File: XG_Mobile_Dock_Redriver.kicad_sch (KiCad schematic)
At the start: 158 parts, among them J1 5-1775443-8, J13 39301240, J14 I2C1, J2 20455-040E-76, J3 20455-040E-76, J6 455860005, J7 10147430-113T0LF, SW1 SW_Push, U1 DS320PR810NJXR, U2 DS320PR810NJXR

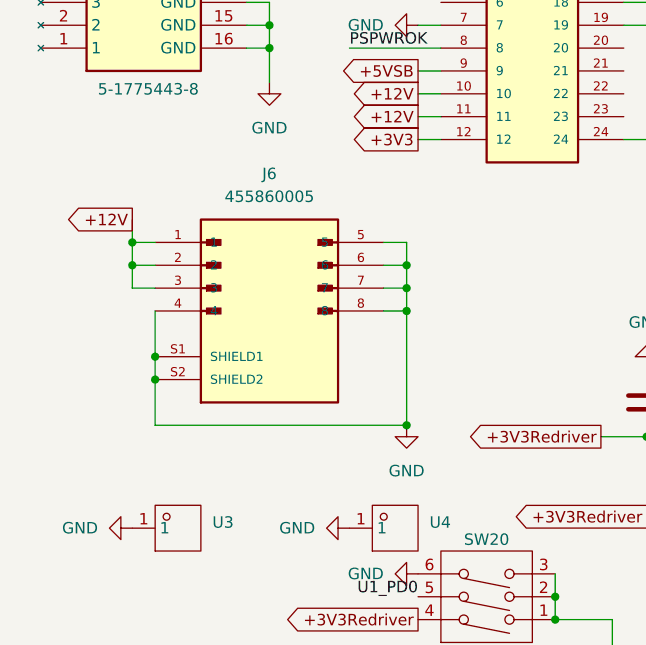
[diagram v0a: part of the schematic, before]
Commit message: added eps connector
added eps connector
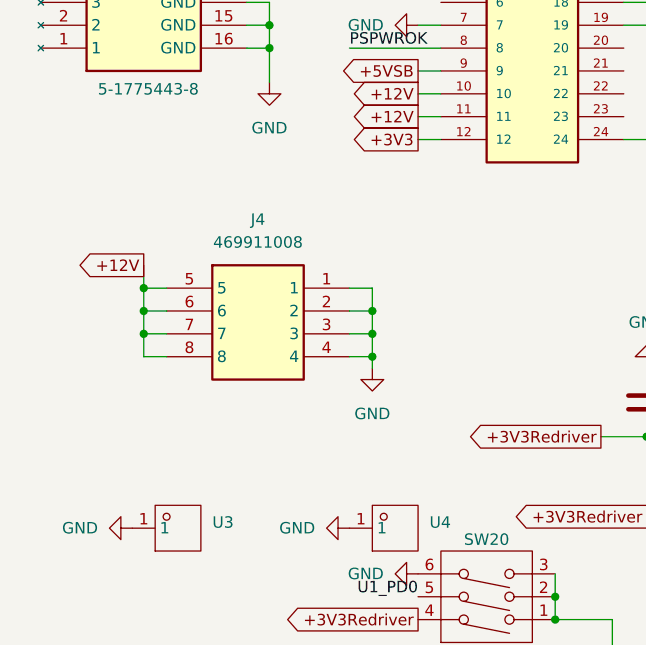
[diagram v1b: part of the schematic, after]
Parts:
- removed J6: 455860005, 455860005:MOLEX_455860005, symbol 455860005:455860005
- added J4: 469911008, 469911008:CON_469911008, symbol 3-1775099-2:3-1775099-2
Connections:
- net +12V: now also J4.5, J4.6, J4.7, J4.8
- net GND: now also J4.1, J4.2, J4.3, J4.4

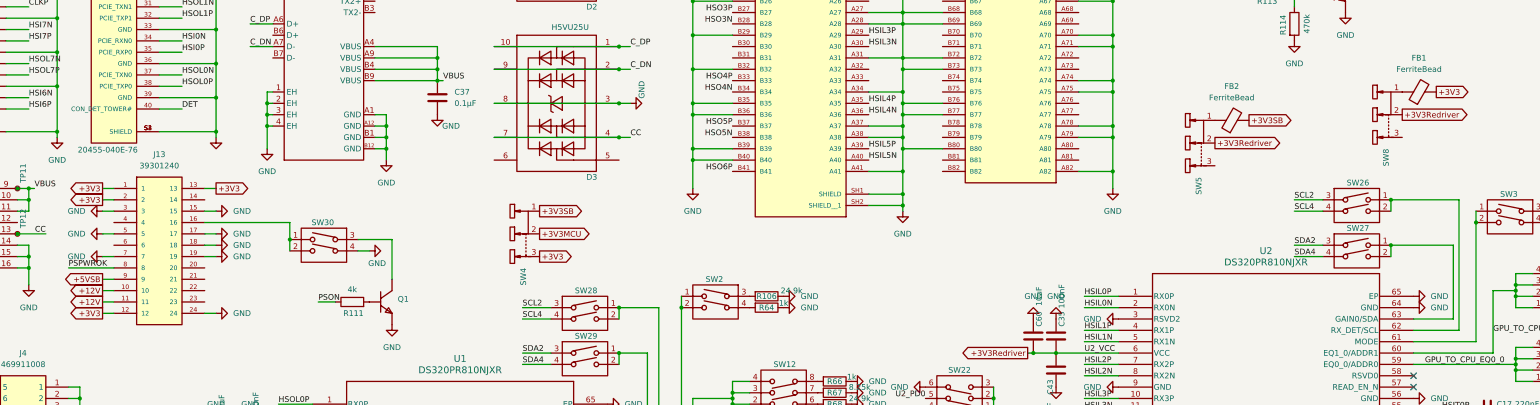
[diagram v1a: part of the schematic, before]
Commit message: added proper voltage config to redrivers
added proper voltage config to redrivers
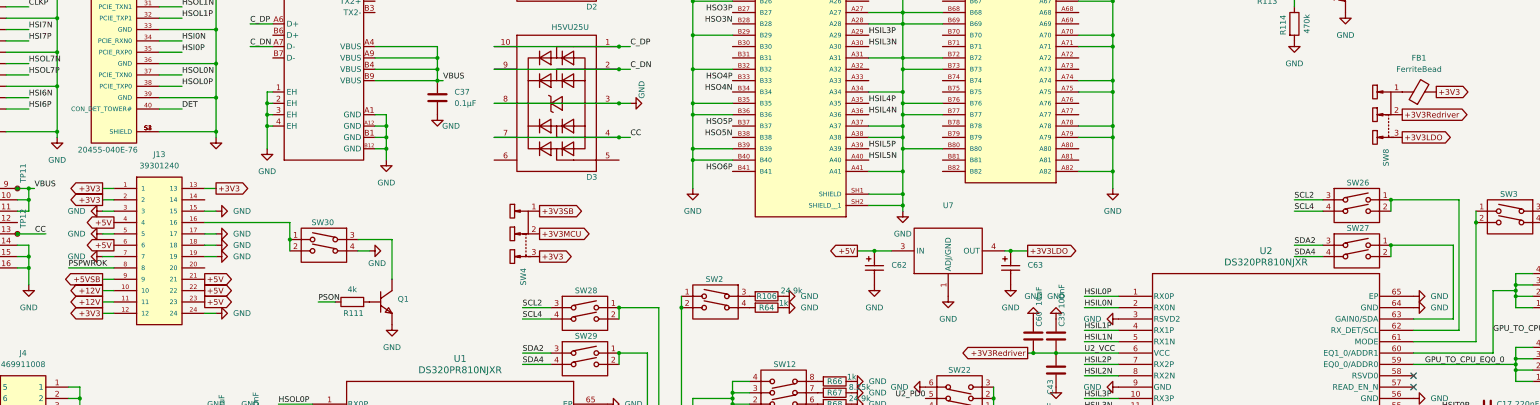
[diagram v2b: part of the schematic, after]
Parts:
- removed FB2: FerriteBead, Resistor_SMD:R_1206_3216Metric, symbol Device:FerriteBead
- removed SW5: ~, SS-12D10L5:SW-TH_SS-12D10L5, symbol SS-12D10L5:SS-12D10L5
- added C62, C63: 10uF, TAJA106K016RNJ:CAP-SMD_L3.2-W1.6-RD-C7171, symbol TAJA106K016RNJ:TAJA106K016RNJ
- added U7: ~, LD1085D2T33R:TO-263-2_L10.0-W9.1-P5.08-LS15.2-TL, symbol LD1085D2T33R:LD1085D2T33R
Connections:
- net GND: now also C62.2, C63.2, U7.1 (ADJ/GND)
- net +5V: now reaches J13.21
- net +5V: now also J13.22, J13.23, J13.4, J13.6, C62.1, U7.3 (IN)
- net +3V3LDO: now reaches SW8.3
- net +3V3LDO: now also C63.1, U7.4 (OUT)

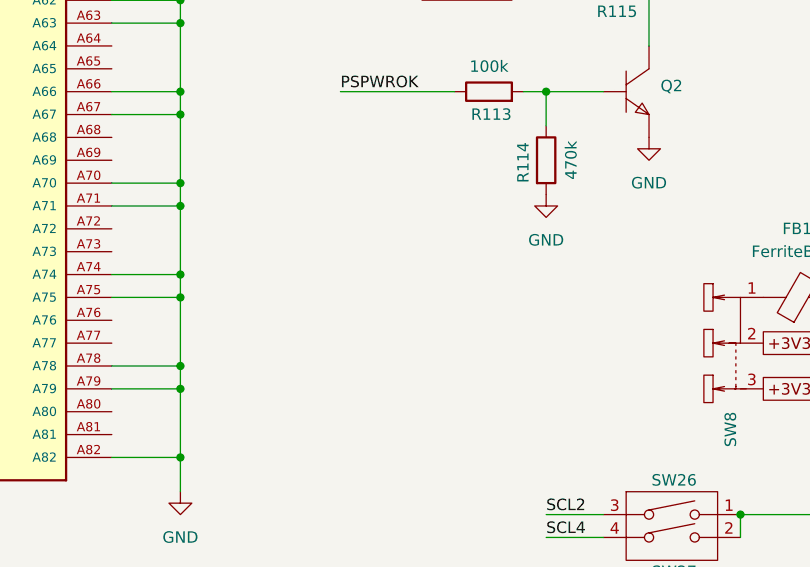
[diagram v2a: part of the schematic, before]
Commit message: added led
added led
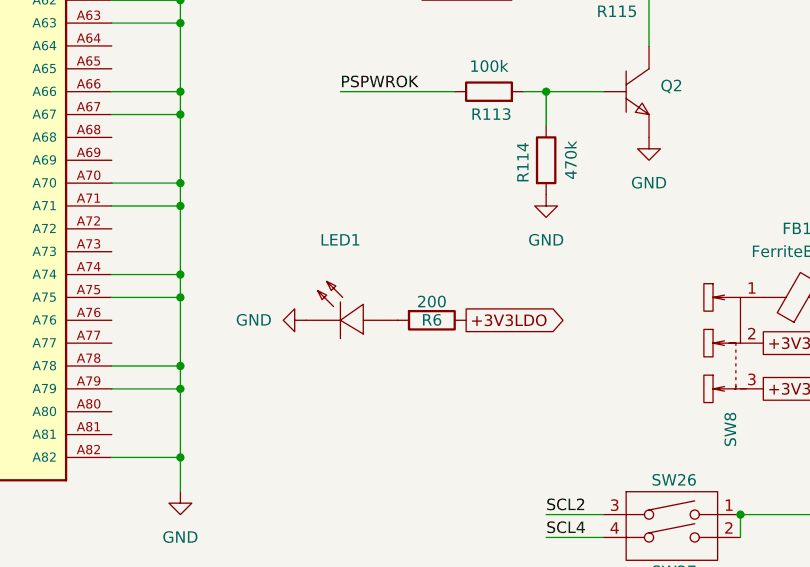
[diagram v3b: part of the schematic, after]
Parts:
- added LED1: ~, KT-0603R:LED0603-RD, symbol KT-0603R:KT-0603R
- added R6: 200, Resistor_SMD:R_0603_1608Metric, symbol Device:R
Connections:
- net +3V3LDO: now also R6.1
- net GND: now also LED1.1 (K)
- new net: LED1.2 (A), R6.2

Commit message: added additional switch
more tweaks
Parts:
- added SW5: ~, SS-12D10L5:SW-TH_SS-12D10L5, symbol SS-12D10L5:SS-12D10L5
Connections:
- net +3V3LDO: now also SW5.3
- net +3V3Redriver: now also SW5.2
- net at FB1.1, SW8.1: now also SW5.1
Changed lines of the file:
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@@
 	)
 	(junction
+		(at 347.98 124.46)
+		(diameter 0)
+		(color 0 0 0 0)
+	)
+	(junction
 		(at 93.98 121.92)
 		(diameter 0)
@@
 	)
 	(junction
+		(at 347.98 119.38)
+		(diameter 0)
+		(color 0 0 0 0)
+	)
+	(junction
 		(at 189.23 73.66)
 		(diameter 0)
@@
 	)
 	(junction
+		(at 347.98 114.3)
+		(diameter 0)
+		(color 0 0 0 0)
+	)
+	(junction
 		(at 381 50.8)
 		(diameter 0)
@@
 	(wire
 		(pts
+			(xy 347.98 116.84) (xy 347.98 119.38)
+		)
+		(stroke
+			(width 0)
+			(type default)
+		)
+	)
+	(wire
+		(pts
 			(xy 189.23 73.66) (xy 198.12 73.66)
 		)
@@
 	(wire
 		(pts
+			(xy 336.55 114.3) (xy 336.55 111.76)
+		)
+		(stroke
+			(width 0)
+			(type default)
+		)
+	)
+	(wire
+		(pts
 			(xy 236.22 43.18) (xy 245.11 43.18)
 		)
@@
 	(wire
 		(pts
+			(xy 336.55 119.38) (xy 336.55 116.84)
+		)
+		(stroke
+			(width 0)
+			(type default)
+		)
+	)
+	(wire
+		(pts
 			(xy 170.18 257.81) (xy 182.88 257.81)
 		)
@@
 	(wire
 		(pts
+			(xy 336.55 124.46) (xy 336.55 121.92)
+		)
+		(stroke
+			(width 0)
+			(type default)
+		)
+	)
+	(wire
+		(pts
 			(xy 80.01 146.05) (xy 82.55 146.05)
 		)
@@
 	(wire
 		(pts
+			(xy 351.79 119.38) (xy 347.98 119.38)
+		)
+		(stroke
+			(width 0)
+			(type default)
+		)
+	)
+	(wire
+		(pts
 			(xy 190.5 232.41) (xy 199.39 232.41)
 		)
@@
 	(wire
 		(pts
+			(xy 347.98 121.92) (xy 347.98 124.46)
+		)
+		(stroke
+			(width 0)
+			(type default)
+		)
+	)
+	(wire
+		(pts
 			(xy 170.18 262.89) (xy 182.88 262.89)
 		)
@@
 	(wire
 		(pts
+			(xy 336.55 111.76) (xy 347.98 111.76)
+		)
+		(stroke
+			(width 0)
+			(type default)
+		)
+	)
+	(wire
+		(pts
 			(xy 267.97 223.52) (xy 267.97 210.82)
 		)
@@
 	(wire
 		(pts
+			(xy 336.55 121.92) (xy 347.98 121.92)
+		)
+		(stroke
+			(width 0)
+			(type default)
+		)
+	)
+	(wire
+		(pts
 			(xy 74.93 57.15) (xy 69.85 57.15)
 		)
@@
 	(wire
 		(pts
+			(xy 347.98 111.76) (xy 347.98 114.3)
+		)
+		(stroke
+			(width 0)
+			(type default)
+		)
+	)
+	(wire
+		(pts
 			(xy 46.99 105.41) (xy 46.99 113.03)
 		)
@@
 	(wire
 		(pts
+			(xy 351.79 124.46) (xy 347.98 124.46)
+		)
+		(stroke
+			(width 0)
+			(type default)
+		)
+	)
+	(wire
+		(pts
 			(xy 74.93 113.03) (xy 69.85 113.03)
 		)
@@
 	(wire
 		(pts
+			(xy 336.55 116.84) (xy 347.98 116.84)
+		)
+		(stroke
+			(width 0)
+			(type default)
+		)
+	)
+	(wire
+		(pts
 			(xy 35.56 29.21) (xy 40.64 29.21)
 		)
@@
 	(global_label "+3V3Redriver"
 		(shape output)
-		(at 347.98 119.38 0)
+		(at 351.79 119.38 0)
 		(fields_autoplaced yes)
 		(effects
@@
 		)
 		(property "Intersheetrefs" "${INTERSHEET_REFS}"
-			(at 363.7862 119.38 0)
+			(at 367.5962 119.38 0)
 			(effects
 				(font
@@
 	(global_label "+3V3LDO"
 		(shape output)
-		(at 347.98 124.46 0)
+		(at 351.79 124.46 0)
 		(fields_autoplaced yes)
 		(effects
@@
 		)
 		(property "Intersheetrefs" "${INTERSHEET_REFS}"
-			(at 359.6738 124.46 0)
+			(at 363.4838 124.46 0)
 			(effects
 				(font
@@
 					(unit 1)
 				)
+			)
+		)
+	)
+	(symbol
+		(lib_id "SS-12D10L5:SS-12D10L5")
+		(at 334.01 119.38 270)
+		(unit 1)
+		(exclude_from_sim no)
+		(in_bom yes)
+		(on_board yes)
+		(dnp no)
+		(fields_autoplaced yes)
+		(property "Reference" "SW5"
+			(at 332.9306 127 0)
+			(effects
+				(font
+					(size 1.27 1.27)
+				)
+				(justify left)
+			)
+		)
+		(property "Value" "~"
+			(at 331.0255 127 0)
+			(effects
+				(font
+					(size 1.27 1.27)
+				)
+				(justify left)
+			)
+		)
+		(property "Footprint" "SS-12D10L5:SW-TH_SS-12D10L5"
+			(at 334.01 119.38 0)
+			(effects
+				(font
+					(size 1.27 1.27)
+				)
+				(hide yes)
+			)
+		)
+		(property "Datasheet" "https://item.szlcsc.com/datasheet/SS-12D10L5/300104.html"
+			(at 334.01 119.38 0)
+			(effects
+				(font
+					(size 1.27 1.27)
+				)
+				(hide yes)
+			)
+		)
+		(property "Description" "Circuit:SPDT Actuator Style:Rectangular Columnar Termination Style:PC Pin Length:13mm Width:6.8mm Switch Height:6.4mm Mounting Type:Through Hole Actuator Color:Black Current Rating:3A Voltage Rating:125V Life:10,000 Cycles Operating Temperature:-40°C~+85°C"
+			(at 334.01 119.38 0)
+			(effects
+				(font
+					(size 1.27 1.27)
+				)
+				(hide yes)
+			)
+		)
+		(property "Part_Number" "SS-12D10L5"
+			(at 334.01 119.38 0)
+			(effects
+				(font
+					(size 1.27 1.27)
+				)
+				(hide yes)
+			)
+		)
+		(property "Manufacturer" "XKB Connection(中国星坤)"
+			(at 334.01 119.38 0)
+			(effects
+				(font
+					(size 1.27 1.27)
+				)
+				(hide yes)
+			)
+		)
+		(property "LCSC" "C319012"
+			(at 334.01 119.38 0)
+			(effects
+				(font
+					(size 1.27 1.27)
+				)
+				(hide yes)
+			)
+		)
+		(pin "3"
+		)
+		(pin "1"
+		)
+		(pin "2"
+		)
+		(instances
+			(project "XG_Mobile_Dock_Redriver"
+				(path "/f97e6956-ab08-42cb-8fed-03fa58e87f0e"
+					(reference "SW5")
+					(unit 1)
+				)

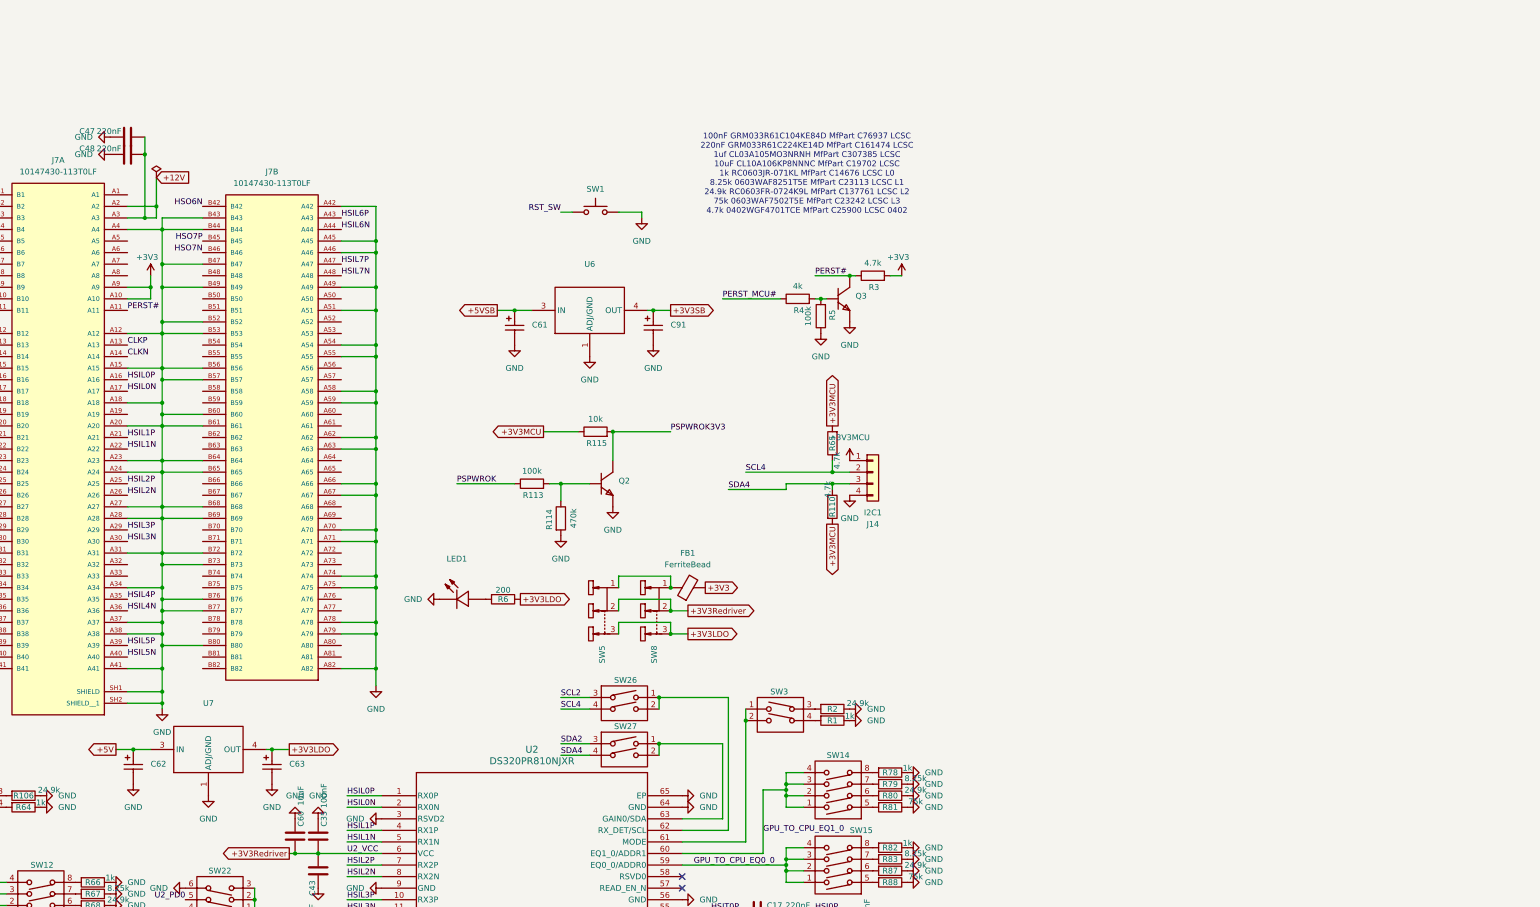
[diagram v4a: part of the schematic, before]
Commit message: started to add better ldo
started to add better ldo
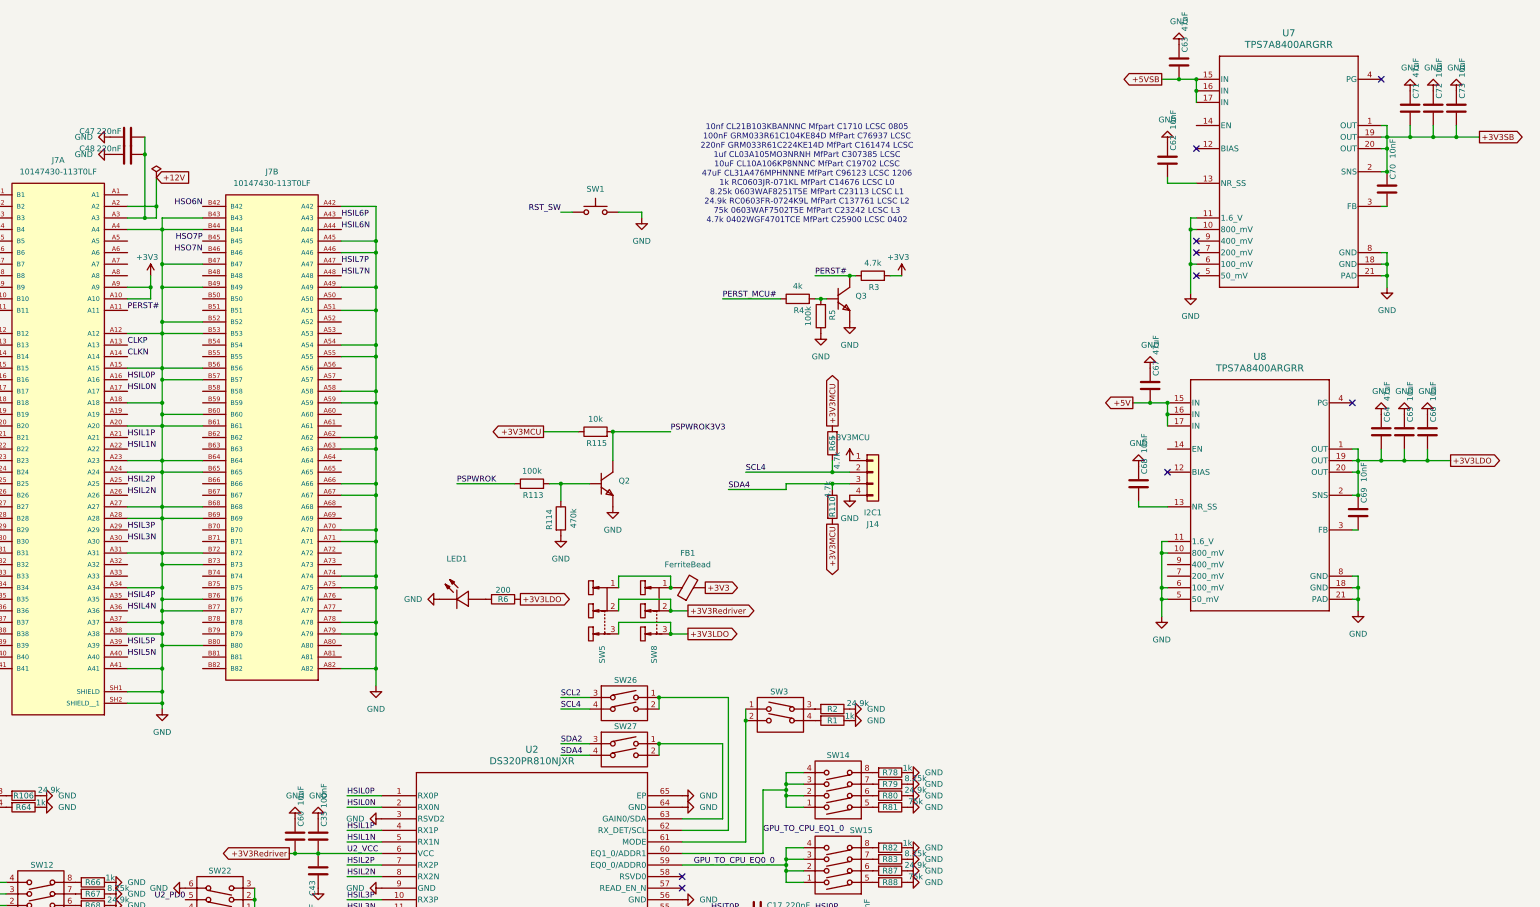
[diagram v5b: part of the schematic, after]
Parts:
- removed C61, C62, C63, C91: 10uF, TAJA106K016RNJ:CAP-SMD_L3.2-W1.6-RD-C7171, symbol TAJA106K016RNJ:TAJA106K016RNJ
- removed U6, U7: ~, LD1085D2T33R:TO-263-2_L10.0-W9.1-P5.08-LS15.2-TL, symbol LD1085D2T33R:LD1085D2T33R
- added C62, C68, C69, C70: 10nF, Capacitor_SMD:C_0805_2012Metric, symbol Device:C
- added C63, C64, C67, C71: 47uF, Capacitor_SMD:C_1206_3216Metric, symbol Device:C
- added C65, C66, C72, C73: 10uF, Capacitor_SMD:C_0603_1608Metric, symbol Device:C
- added U7, U8: TPS7A8400ARGRR, TPS7A8400A:RGR0020A, symbol TPS7A8400ARGRR:TPS7A8400ARGRR
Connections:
- net +3V3LDO: now also C64.2, C65.2, C66.2, C69.1, U8.1 (OUT), U8.19 (OUT), U8.2 (SNS), U8.20 (OUT)
- net +3V3SB: now also C70.1, C71.2, C72.2, C73.2, U7.1 (OUT), U7.19 (OUT), U7.2 (SNS), U7.20 (OUT)
- net +5V: now also C67.2, U8.15 (IN), U8.16 (IN), U8.17 (IN)
- net +5VSB: now also C63.2, U7.15 (IN), U7.16 (IN), U7.17 (IN)
- net GND: now also C62.1, C63.1, C64.1, C65.1, C66.1, C67.1, C68.1, C71.1, C72.1, C73.1, U7.10 (800_mV), U7.11 (1.6_V), U7.18 (GND), U7.21 (PAD), U7.6 (100_mV), U7.8 (GND), U8.10 (800_mV), U8.11 (1.6_V), U8.18 (GND), U8.21 (PAD), U8.5 (50_mV), U8.6 (100_mV), U8.8 (GND)
- new net: C62.2, U7.13 (NR_SS)
- new net: C68.2, U8.13 (NR_SS)
- new net: C70.2, U7.3 (FB)
- new net: C69.2, U8.3 (FB)
- no-connect marks 8 -> 15
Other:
- note added: "10nf CL21B103KBANNNC Mfpart C1710 LCSC 0805 100nF GRM033R61C104KE84D MfPart C76937 LCSC 220nF GRM033R61C224KE14D MfPart C161474 LCSC 1uf CL03A105MO3NRNH MfPart C307385 LCSC 10uF CL10A106KP8NNNC MfPart C19702 LCSC 47uF CL31A476MPHNNNE MfPart C96123 LCSC 1206 1k RC0603JR-071KL MfPart C14676 LCSC L0 8.25k 0603WAF8251T5E MfPart C23113 LCSC L1 24.9k RC0603FR-0724K9L MfPart C137761 LCSC L2 75k 0603WAF7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"
- note removed: "100nF GRM033R61C104KE84D MfPart C76937 LCSC 220nF GRM033R61C224KE14D MfPart C161474 LCSC 1uf CL03A105MO3NRNH MfPart C307385 LCSC 10uF CL10A106KP8NNNC MfPart C19702 LCSC 1k RC0603JR-071KL MfPart C14676 LCSC L0 8.25k 0603WAF8251T5E MfPart C23113 LCSC L1 24.9k RC0603FR-0724K9L MfPart C137761 LCSC L2 75k 0603WAF7502T5E MfPart C23242 LCSC L3 4.7k 0402WGF4701TCE MfPart C25900 LCSC 0402"
